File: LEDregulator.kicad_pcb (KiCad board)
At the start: 2 copper layers, 43.2 x 57.1 mm, 36 parts, among them J1 2.1mm DC jack, J2 2way Screw Terminal, J3 2way Screw Terminal, SW1 DPDT Switch, SW2 6pos rotary

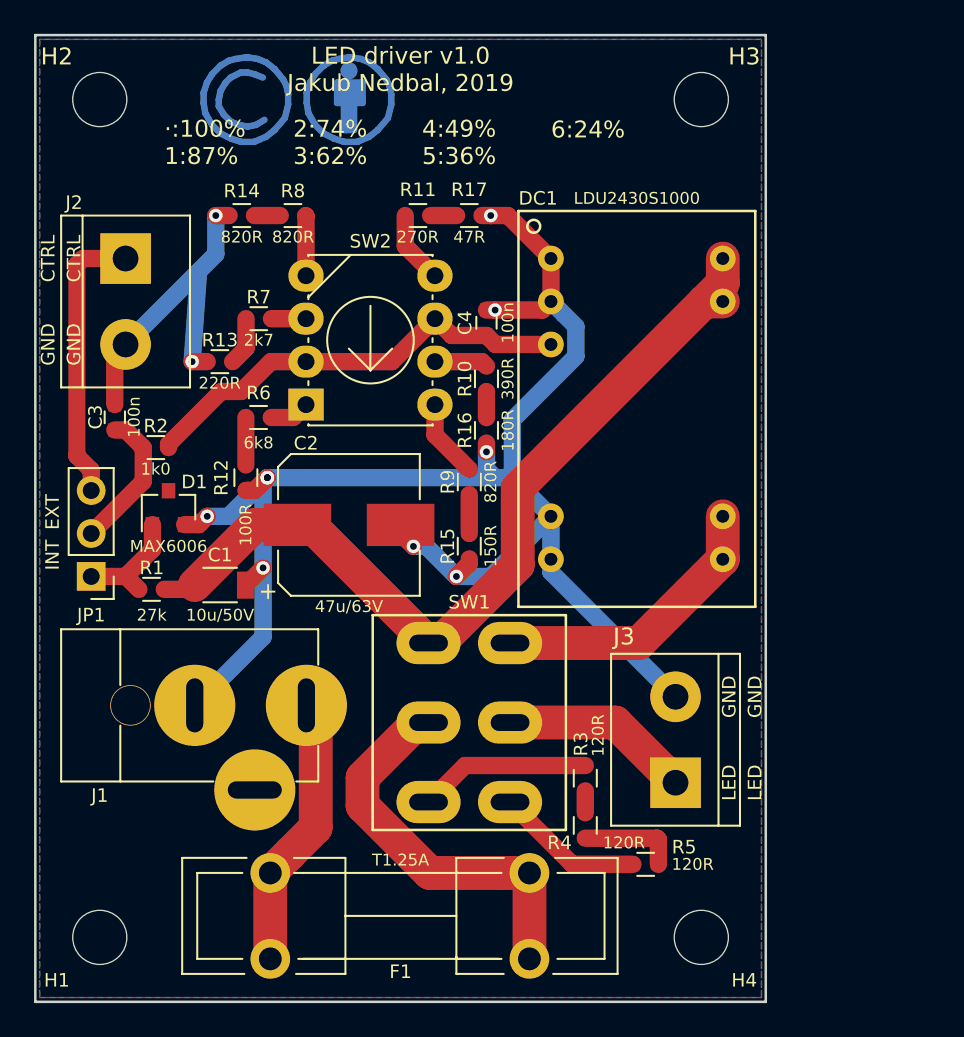
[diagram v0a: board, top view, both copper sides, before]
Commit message: Started a new branch (v1.1) that has got fan control, low-side switch on the LED for trickle current and power resistors. Also the 5.08mm terminal connectors have been changed to more compact 3.81mm.
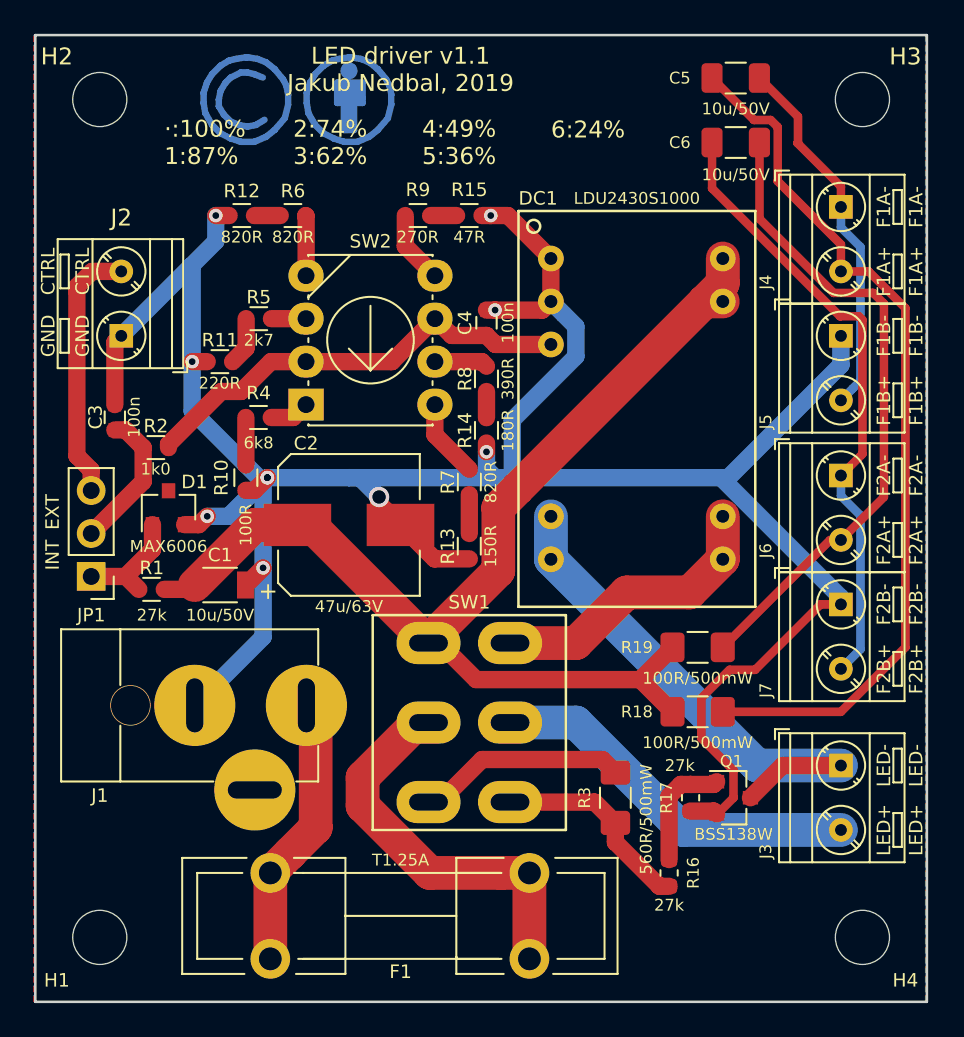
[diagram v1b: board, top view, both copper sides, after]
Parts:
- removed the R4 at (150.6, 84.8)
- removed the R5 at (154.2, 87.1)
- added C5: 10u/50V, Capacitor_SMD:C_1206_3216Metric, F.Cu at (159.5, 40.6)
- added C6: 10u/50V, Capacitor_SMD:C_1206_3216Metric, F.Cu at (159.5, 44.5)
- added J4: 2way Screw Terminal, TerminalBlock_MetzConnect:TerminalBlock_MetzConnect_Type086_RT03402HBLC_1x02_P3.81mm_Horizontal, F.Cu at (165.7, 48.3)
- added J5: 2way Screw Terminal, TerminalBlock_MetzConnect:TerminalBlock_MetzConnect_Type086_RT03402HBLC_1x02_P3.81mm_Horizontal, F.Cu at (165.7, 55.9)
- added J6: 2way Screw Terminal, TerminalBlock_MetzConnect:TerminalBlock_MetzConnect_Type086_RT03402HBLC_1x02_P3.81mm_Horizontal, F.Cu at (165.7, 64.1)
- added J7: 2way Screw Terminal, TerminalBlock_MetzConnect:TerminalBlock_MetzConnect_Type086_RT03402HBLC_1x02_P3.81mm_Horizontal, F.Cu at (165.7, 71.8)
- added Q1: BSS138W, Package_TO_SOT_SMD:SOT-23, F.Cu at (159.4, 83.2)
- added R16: 27k, Resistor_SMD:R_0603_1608Metric, F.Cu at (155.6, 87.6)
- added R17: 27k, Resistor_SMD:R_0603_1608Metric, F.Cu at (156.8, 83.2)
- added R18: 100R/500mW, Resistor_SMD:R_1206_3216Metric_Pad1.42x1.75mm_HandSolder, F.Cu at (157.3, 78.1)
- added R19: 100R/500mW, Resistor_SMD:R_1206_3216Metric_Pad1.42x1.75mm_HandSolder, F.Cu at (157.3, 74.3)
- J2, J3: footprint Terminal_Blocks:TerminalBlock_bornier-2_P5.08mm -> TerminalBlock_MetzConnect:TerminalBlock_MetzConnect_Type086_RT03402HBLC_1x02_P3.81mm_Horizontal
- R3: value 120R -> 560R/500mW; footprint Resistors_SMD:R_0603 -> Resistor_SMD:R_1206_3216Metric_Pad1.42x1.75mm_HandSolder
- moved J3 9.83 mm to (165.7, 81.3), turned to 270 degrees
- moved H3 9.53 mm to (167.0, 41.9)
- moved H4 9.53 mm to (167.0, 91.4)
- moved J2 4.58 mm to (123.2, 55.9), turned to 90 degrees
- moved R3 2.12 mm to (152.4, 83.2)
- renumbered R12 to R10, R13 to R11, R14 to R12, R15 to R13, R16 to R14, R17 to R15, R6 to R4, R7 to R5, R8 to R6, R9 to R7, R10 to R8, R11 to R9
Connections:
- net /+24V renamed /+30V
- net /+24V_DriverSupply renamed +VDC
- net /+24V_TrickleSupply renamed /+30V_TrickleSupply
- DC1 pad 7: GND -> /LEDout-
- DC1 pad 8: GND -> /LEDout-
- J1 pad 3: (no net) -> Net-(J1-Pad3)
- J2 pad 1: /ExtCtrl -> GND
- J2 pad 2: GND -> /ExtCtrl
- J3 pad 1: /LEDout -> /LEDout-
- J3 pad 2: GND -> /LEDout+
- R3 pad 1: Net-(R3-Pad1) -> /TrickleOut
- SW1 pad 5: /LEDout -> /LEDout+
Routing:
- net Net-(C5-Pad1): track 0.00 -> 52.3 mm
- net GND: track 115.9 -> 158.8 mm, vias 12 -> 10
- net Net-(C6-Pad1): track 0.00 -> 38.6 mm
- net Net-(C6-Pad2): track 0.00 -> 36.9 mm
- net /LEDout-: track 0.00 -> 30.9 mm
- net /LEDout+: track 0.00 -> 22.2 mm
- net Net-(C5-Pad2): track 0.00 -> 22.0 mm
- net +VDC: track 51.5 -> 69.9 mm
- net /LEDout: track 11.3 -> 0.00 mm
- net Net-(Q1-Pad1): track 0.00 -> 6.92 mm
- net Net-(R4-Pad1): track 5.82 -> 0.00 mm
- net /TrickleOut: track 8.79 -> 12.1 mm
- net /+30V_TrickleSupply: track 10.2 -> 12.4 mm
- net /ExtCtrl: track 16.7 -> 15.4 mm
- net Net-(R3-Pad1): track 1.29 -> 0.00 mm
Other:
- board size 43.2 x 57.1 mm -> 52.7 x 57.1 mm
- board text added: "F1A+"
- board text added: "F1A-"
- board text added: "F1B+"
- board text added: "F1B-"
- board text added: "F2A+"
- board text added: "F2A-"
- board text added: "F2B+"
- board text added: "F2B-"
- board text added: "LED driver v1.1 Jakub Nedbal, 2019"
- board text added: "LED+"
- board text added: "LED-"
- board text removed: "LED"
- board text removed: "LED driver v1.0 Jakub Nedbal, 2019"

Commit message: 3D models ready
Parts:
- turned C6 to 0 degrees
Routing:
- net Net-(C6-Pad2): track 36.9 -> 34.4 mm
- net Net-(C6-Pad1): track 38.6 -> 36.3 mm
